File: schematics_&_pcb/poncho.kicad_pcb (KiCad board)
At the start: 2 copper layers, 9 parts, among them J1 TB_1X2, J2 TB_1X2, J3 TB_1X2, P1 CONN_20X2, P2 CONN_20X2, P3 ESP8266

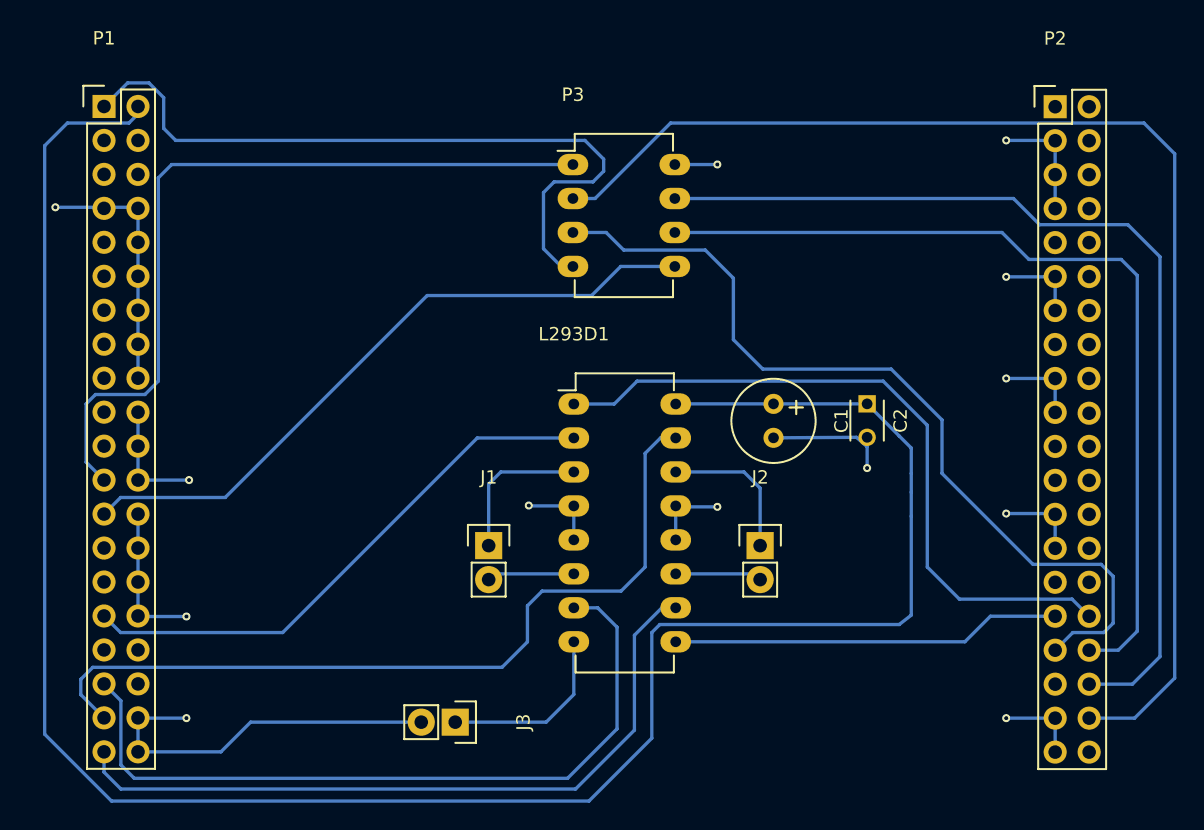
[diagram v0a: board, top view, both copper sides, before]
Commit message: Correciones en el PCB: tamaño de las coronas, pads para vias, ancho de los tracks.
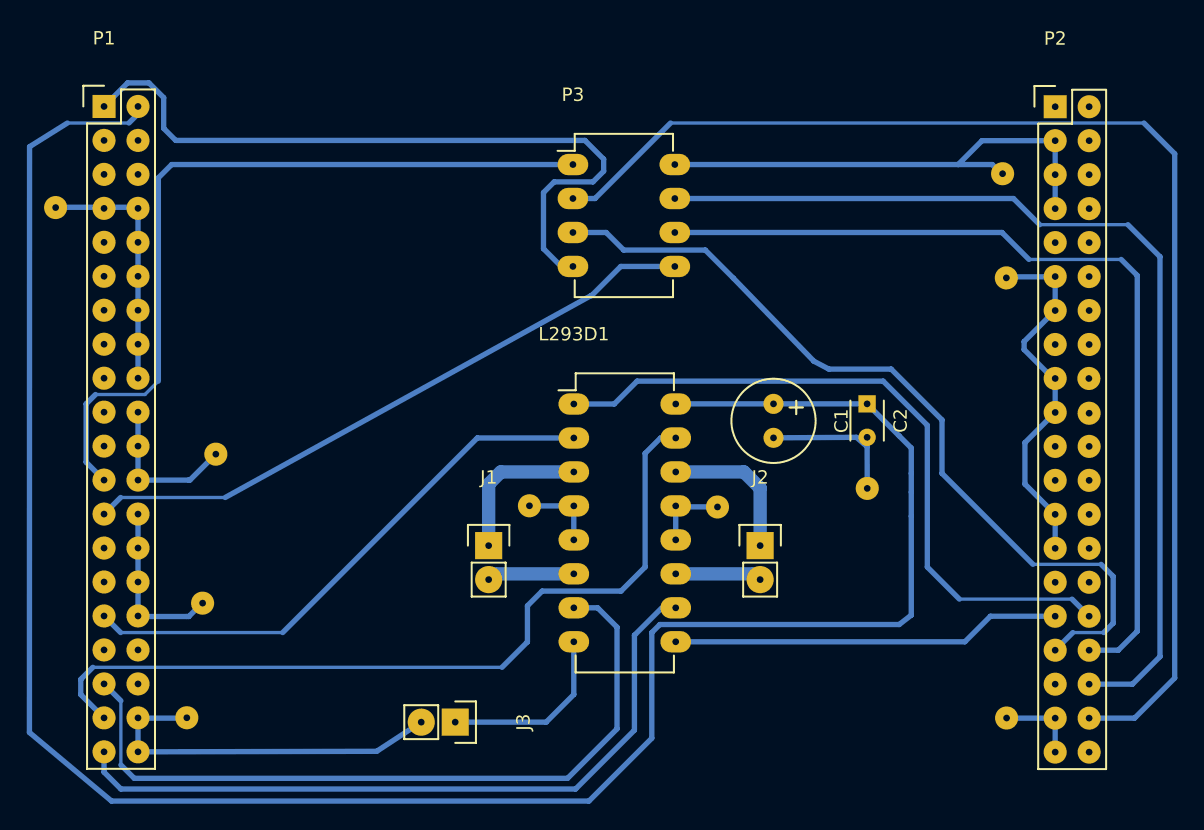
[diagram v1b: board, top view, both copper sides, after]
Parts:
- added REF**: SolderWirePad_single_1mmDrill, Wire_Pads:SolderWirePad_single_1mmDrill, F.Cu at (170.3, 61.8)
- added REF**: SolderWirePad_single_1mmDrill, Wire_Pads:SolderWirePad_single_1mmDrill, F.Cu at (104.8, 71.5)
- added REF**: SolderWirePad_single_1mmDrill, Wire_Pads:SolderWirePad_single_1mmDrill, F.Cu at (175.9, 76.8)
- added REF**: SolderWirePad_single_1mmDrill, Wire_Pads:SolderWirePad_single_1mmDrill, F.Cu at (175.9, 109.7)
- added REF**: SolderWirePad_single_1mmDrill, Wire_Pads:SolderWirePad_single_1mmDrill, F.Cu at (140.2, 93.8)
- added REF**: SolderWirePad_single_1mmDrill, Wire_Pads:SolderWirePad_single_1mmDrill, F.Cu at (154.3, 93.9)
- added REF**: SolderWirePad_single_1mmDrill, Wire_Pads:SolderWirePad_single_1mmDrill, F.Cu at (165.5, 92.5)
- added REF**: SolderWirePad_single_1mmDrill, Wire_Pads:SolderWirePad_single_1mmDrill, F.Cu at (115.8, 101.1)
- added REF**: SolderWirePad_single_1mmDrill, Wire_Pads:SolderWirePad_single_1mmDrill, F.Cu at (114.6, 109.7)
- added REF**: SolderWirePad_single_1mmDrill, Wire_Pads:SolderWirePad_single_1mmDrill, F.Cu at (116.8, 90.0)
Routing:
- net GND: track 105.7 -> 146.3 mm, vias 12 -> 9
- net /GPIO4: track 64.8 -> 62.0 mm
- net /RS232_TXD: track 50.4 -> 48.0 mm
- net +5V: track 161.2 -> 162.9 mm
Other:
- net class Default: trace_width 0.25 -> 0.2
- net class Motors added: clearance 0.2, trace_width 1, via_dia 0.6, via_drill 0.4
- net class ThickerTracks added: clearance 0.2, trace_width 0.4, via_dia 0.6, via_drill 0.4
- rule via_min_size: 0.4 -> 0.5

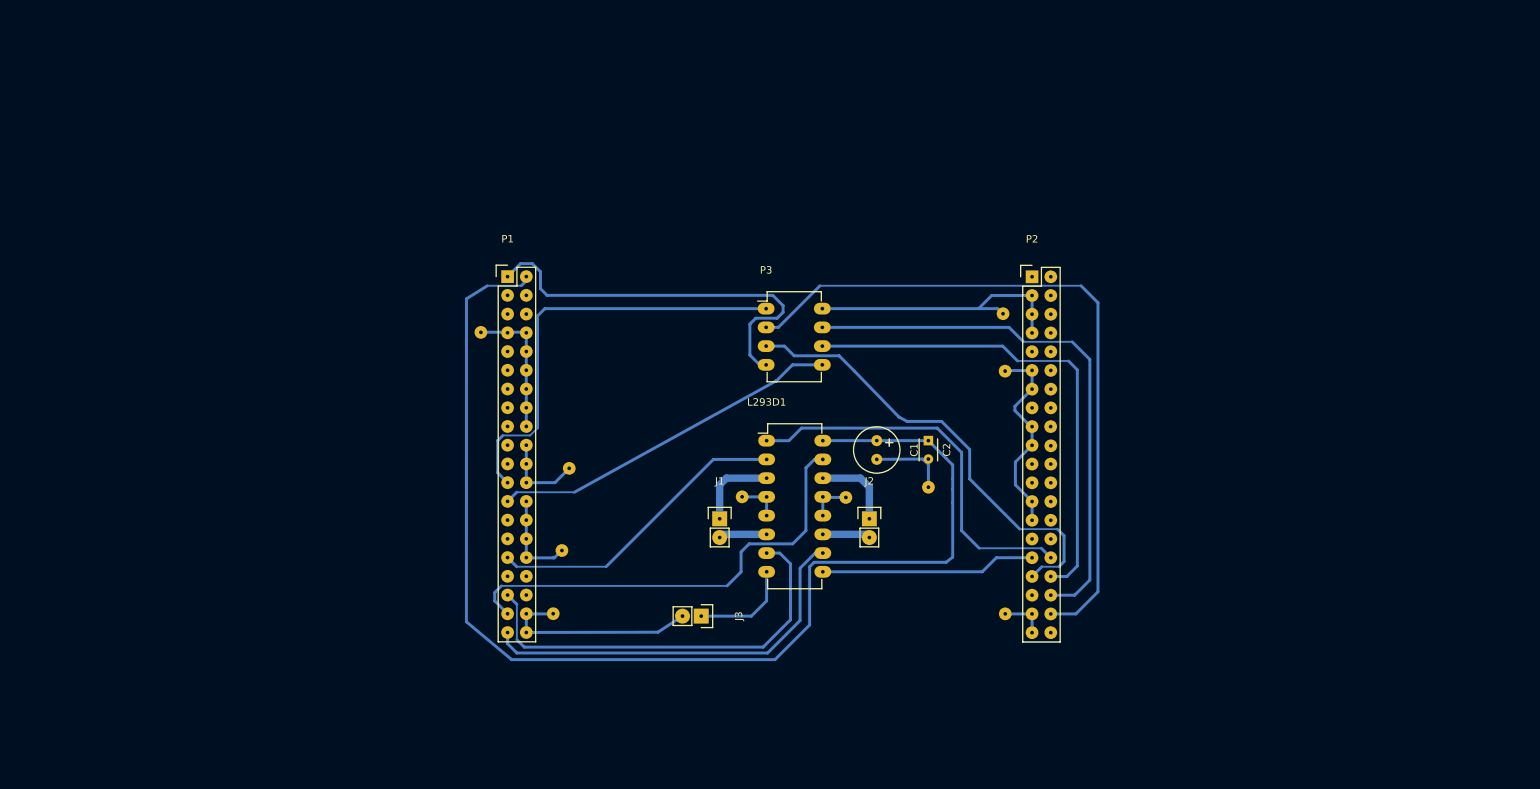
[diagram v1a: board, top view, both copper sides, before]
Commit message: PCB modificado. [TODO] Verificar que esté correcto y proceder a armar la placa.
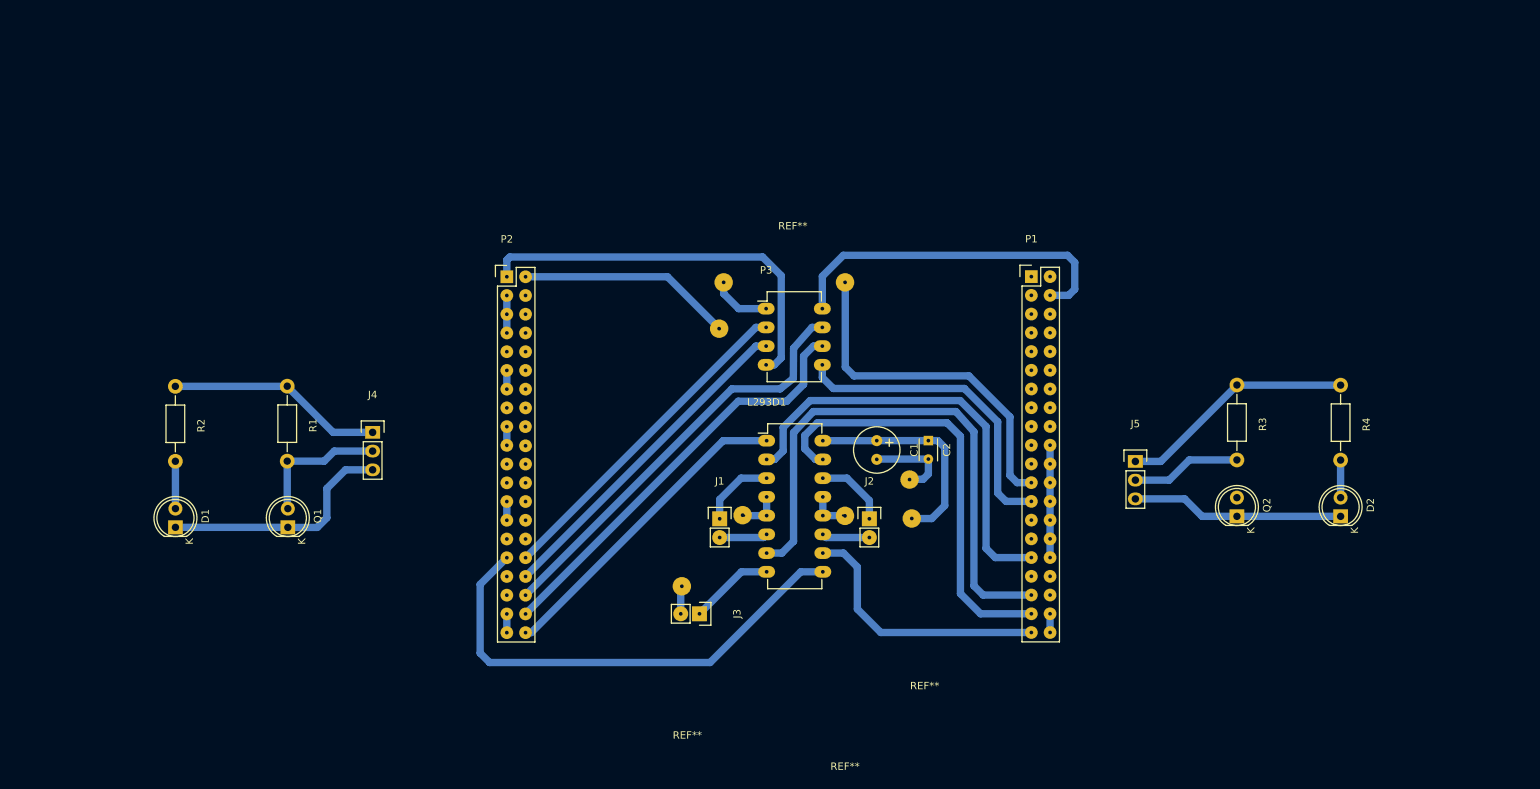
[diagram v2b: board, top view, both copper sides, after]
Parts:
- removed the REF** at (170.3, 61.8)
- removed the REF** at (104.8, 71.5)
- removed the REF** at (175.9, 76.8)
- removed the REF** at (175.9, 109.7)
- removed the REF** at (140.2, 93.8)
- removed the REF** at (165.5, 92.5)
- removed the REF** at (115.8, 101.1)
- removed the REF** at (114.6, 109.7)
- removed the REF** at (116.8, 90.0)
- added D1: LED, LEDs:LED-5MM, F.Cu at (63.4, 98.0)
- added D2: LED, LEDs:LED-5MM, F.Cu at (221.4, 96.5)
- added J4: TB_1X3, Pin_Headers:Pin_Header_Straight_1x03, F.Cu at (90.1, 85.1)
- added J5: TB_1X3, Pin_Headers:Pin_Header_Straight_1x03, F.Cu at (193.6, 89.0)
- added Q1: NPN-PHOTO-2, LEDs:LED-5MM, F.Cu at (78.6, 98.0)
- added Q2: NPN-PHOTO-2, LEDs:LED-5MM, F.Cu at (207.3, 96.5)
- added R1: 4700, Resistors_ThroughHole:Resistor_Horizontal_RM10mm, F.Cu at (78.6, 83.9)
- added R2: 100, Resistors_ThroughHole:Resistor_Horizontal_RM10mm, F.Cu at (63.4, 83.9)
- added R3: 4700, Resistors_ThroughHole:Resistor_Horizontal_RM10mm, F.Cu at (207.3, 83.7)
- added R4: 100, Resistors_ThroughHole:Resistor_Horizontal_RM10mm, F.Cu at (221.4, 83.8)
- added REF**: WireConnection_1mmDrill, Wire_Connections_Bridges:WireConnection_1.00mmDrill, F.Cu at (142.3, 56.9)
- added REF**: WireConnection_1mmDrill, Wire_Connections_Bridges:WireConnection_1.00mmDrill, F.Cu at (160.2, 119.2)
- added REF**: WireConnection_1mmDrill, Wire_Connections_Bridges:WireConnection_1.00mmDrill, F.Cu at (128.0, 126.0)
- added REF**: WireConnection_1mmDrill, Wire_Connections_Bridges:WireConnection_1.00mmDrill, F.Cu at (149.3, 130.2)
- moved P2 71.2 mm to (108.3, 64.0)
- moved P1 71.0 mm to (179.5, 64.0)
- moved J3 0.40 mm to (134.5, 109.7)
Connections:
- L293D1 pad 1: /GPIO1 -> /GPIO8
- P3 pad 2: /GPIO7 -> /GPIO1
- P3 pad 3: /GPIO4 -> /GPIO3
- P3 pad 6: /GPIO3 -> /GPIO7
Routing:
- net +5V: track 162.9 -> 59.1 mm, vias 0 -> 2
- net /GPIO4: track 62.0 -> 0.00 mm
- net +3V3: track 54.8 -> 115.7 mm
- net /GPIO8: track 0.00 -> 43.5 mm
- net /GPIO7: track 95.1 -> 57.5 mm
- net /GPIO2: track 29.2 -> 66.5 mm
- net GND: track 146.3 -> 168.2 mm, vias 9 -> 4
- net /GPIO3: track 66.7 -> 45.6 mm
- net GNDA: track 18.9 -> 0.00 mm, vias 1 -> 0
- net /GPIO0: track 0.00 -> 18.6 mm
- net /TEC_COL0: track 54.6 -> 36.1 mm
- net /TEC_F3: track 57.1 -> 75.2 mm
- net /TEC_COL1: track 41.7 -> 59.6 mm
- net /GPIO5: track 74.1 -> 57.7 mm
- net /TEC_COL2: track 0.00 -> 14.9 mm
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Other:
- net class Default: clearance 0.2 -> 0.25; trace_width 0.2 -> 1
- net class Motors removed
- net class ThickerTracks removed
- rule trace_clearance: 0.2 -> 0.25

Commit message: .pcb y .sch modificados.
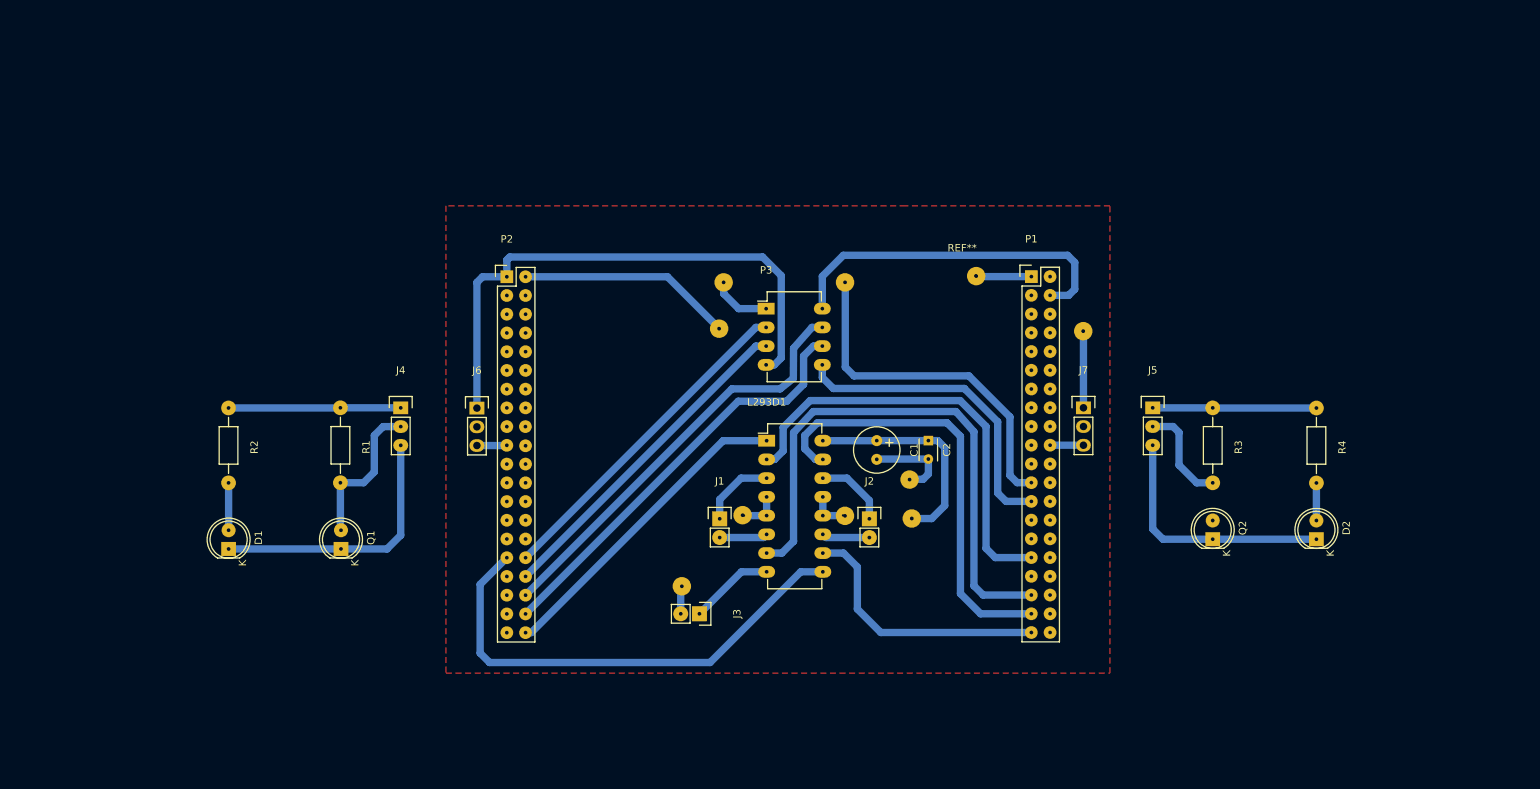
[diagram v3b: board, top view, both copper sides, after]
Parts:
- added J6: TB_1X3, Pin_Headers:Pin_Header_Straight_1x03, F.Cu at (104.3, 81.8)
- added J7: TB_1X3, Pin_Headers:Pin_Header_Straight_1x03, F.Cu at (186.5, 81.8)
- added REF**: SolderWirePad_2x_1-2mmDrill, Wire_Pads:SolderWirePad_2x_1-2mmDrill, F.Cu at (170.1, 63.9)
- moved D1 7.78 mm to (70.6, 100.9)
- moved Q1 7.78 mm to (85.8, 100.9)
- moved R1 7.78 mm to (85.8, 86.8)
- moved R2 7.78 mm to (70.6, 86.8)
- moved J5 7.64 mm to (195.9, 81.8)
- moved J4 5.05 mm to (94.0, 81.8)
- moved R3 4.51 mm to (204.1, 86.8)
- moved D2 4.51 mm to (218.1, 99.6)
- moved Q2 4.51 mm to (204.1, 99.6)
- moved R4 4.51 mm to (218.1, 86.9)
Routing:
- net (no net): track 0.00 -> 18.0 mm, vias 0 -> 2
- net GND: track 168.2 -> 153.2 mm
- net +3V3: track 115.7 -> 121.2 mm
- net /GPIO0: track 18.6 -> 20.7 mm
- net /TEC_COL2: track 14.9 -> 13.9 mm
- added copper zone on F.Cu, net GND

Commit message: Modificación del footprint del ESP8266, posición y conexión de los encoders.
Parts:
- added REF**: SolderWirePad_2x_2mmDrill, Wire_Pads:SolderWirePad_2x_2mmDrill, F.Cu at (170.9, 39.6)
- added REF**: SolderWirePad_2x_2mmDrill, Wire_Pads:SolderWirePad_2x_2mmDrill, F.Cu at (194.4, 39.8)
- P3: footprint Housings_DIP:DIP-8_W7.62mm_LongPads -> Pin_Headers:Pin_Header_Straight_2x04
- moved D2 10.9 mm to (229.1, 99.6)
- moved R4 10.9 mm to (229.1, 86.9)
- moved R2 9.83 mm to (60.8, 86.8)
- moved D1 9.76 mm to (60.9, 100.9)
- moved P3 3.10 mm to (145.7, 66.2)
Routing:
- net /GPIO1: track 45.6 -> 77.4 mm
- net GND: track 153.2 -> 184.2 mm
- net +3V3: track 121.2 -> 149.9 mm
- net /TEC_COL2: track 13.9 -> 41.7 mm
- net /GPIO0: track 20.7 -> 44.1 mm
- net /RS232_TXD: track 42.7 -> 56.4 mm
- net /GPIO7: track 57.5 -> 44.0 mm, vias 0 -> 2
- net /RS232_RXD: track 56.0 -> 48.8 mm
- net /GPIO3: track 45.6 -> 52.0 mm
- net /GPIO5: track 57.7 -> 59.7 mm, vias 0 -> 2
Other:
- board text added: "Emiliano Liotta Federico Bouche Julián Ailán Lucas Hourquebie UNLP - 2015"

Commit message: Poncho modificado a dos capas.
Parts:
- removed the REF** at (142.3, 56.9)
- removed the REF** at (160.2, 119.2)
- removed the REF** at (128.0, 126.0)
- removed the REF** at (149.3, 130.2)
- removed the REF** at (170.1, 63.9)
- removed the REF** at (170.9, 39.6)
- removed the REF** at (194.4, 39.8)
- added REF**: SolderWirePad_single_1mmDrill, Wire_Pads:SolderWirePad_single_1mmDrill, F.Cu at (162.0, 68.5)
- added REF**: SolderWirePad_single_1mmDrill, Wire_Pads:SolderWirePad_single_1mmDrill, F.Cu at (158.5, 66.0)
- added REF**: SolderWirePad_single_1mmDrill, Wire_Pads:SolderWirePad_single_1mmDrill, F.Cu at (152.4, 63.6)
- added REF**: SolderWirePad_single_1mmDrill, Wire_Pads:SolderWirePad_single_1mmDrill, F.Cu at (165.5, 91.7)
- added REF**: SolderWirePad_single_1mmDrill, Wire_Pads:SolderWirePad_single_1mmDrill, F.Cu at (154.5, 93.8)
- added REF**: SolderWirePad_single_1mmDrill, Wire_Pads:SolderWirePad_single_1mmDrill, F.Cu at (140.1, 93.8)
- added REF**: SolderWirePad_single_1mmDrill, Wire_Pads:SolderWirePad_single_1mmDrill, F.Cu at (127.1, 109.7)
- added REF**: SolderWirePad_single_1mmDrill, Wire_Pads:SolderWirePad_single_1mmDrill, F.Cu at (186.6, 112.2)
- moved D1 16.2 mm to (44.6, 100.9)
- moved J4 16.2 mm to (77.7, 81.8)
- moved Q1 16.2 mm to (69.6, 100.9)
- moved R1 16.2 mm to (69.5, 86.8)
- moved R2 16.2 mm to (44.5, 86.8)
- moved D2 12.2 mm to (241.3, 99.6)
- moved J5 12.2 mm to (208.2, 81.8)
- moved Q2 12.2 mm to (216.3, 99.6)
- moved R3 12.2 mm to (216.3, 86.8)
- moved R4 12.2 mm to (241.3, 86.9)
- moved P3 2.63 mm to (146.2, 63.6)
- moved J6 0.46 mm to (103.8, 81.8)
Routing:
- net (no net): track 18.0 -> 600.0 mm, vias 2 -> 0
- net GND: track 184.2 -> 43.5 mm, vias 4 -> 6
- net +3V3: track 149.9 -> 93.5 mm
- net /GPIO7: track 44.0 -> 84.9 mm, vias 2 -> 1
- net /GPIO1: track 77.4 -> 51.8 mm
- net /GPIO0: track 44.1 -> 23.2 mm
- net /TEC_F2: track 59.5 -> 39.0 mm
- net /GPIO5: track 59.7 -> 80.1 mm, vias 2 -> 1
- net /TEC_COL2: track 41.7 -> 27.7 mm
- net /RS232_RXD: track 48.8 -> 57.1 mm, vias 2 -> 0
- net +5V: track 59.1 -> 52.3 mm, vias 2 -> 0
- net Net-(D1-Pad2): track 6.45 -> 0.11 mm
- net /RS232_TXD: track 56.4 -> 50.2 mm
- net Net-(D2-Pad2): track 5.09 -> 0.00 mm
- net /TEC_COL0: track 36.1 -> 32.7 mm
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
